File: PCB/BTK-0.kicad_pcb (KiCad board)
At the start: 4 copper layers, 169.2 x 105 mm, 92 parts, among them J1 USB_C_Receptacle_USB2.0_16P, J4 Conn_01x15, J5 Conn_01x15_Socket, SW1 EN, SW10 1,2, SW11 2,2, SW12 3,2, SW13 4,2, SW14 5,2, SW15 6,2, SW16 1,3, SW17 2,3, SW18 3,3, SW19 4,3, SW2 BOOT, SW20 5,3, SW21 6,3, SW22 1,4, SW23 2,4, SW24 3,4, SW25 4,4, SW26 5,4, SW27 6,4, SW28 1,4, SW29 2,4, SW3 RotaryEncoder_Switch_MP, SW30 3,4, SW31 4,4, SW32 5,4, SW33 6,4, SW4 1,1, SW5 2,1, SW6 3,1, SW7 4,1, SW8 5,1, SW9 6,1, U1 NCP1117-3.3_SOT223, U2 NCP1117-3.3_SOT223, U3 USBLC6-2SC6, U4 ESP32-C6-MINI-1, U5 TVS1400DRV

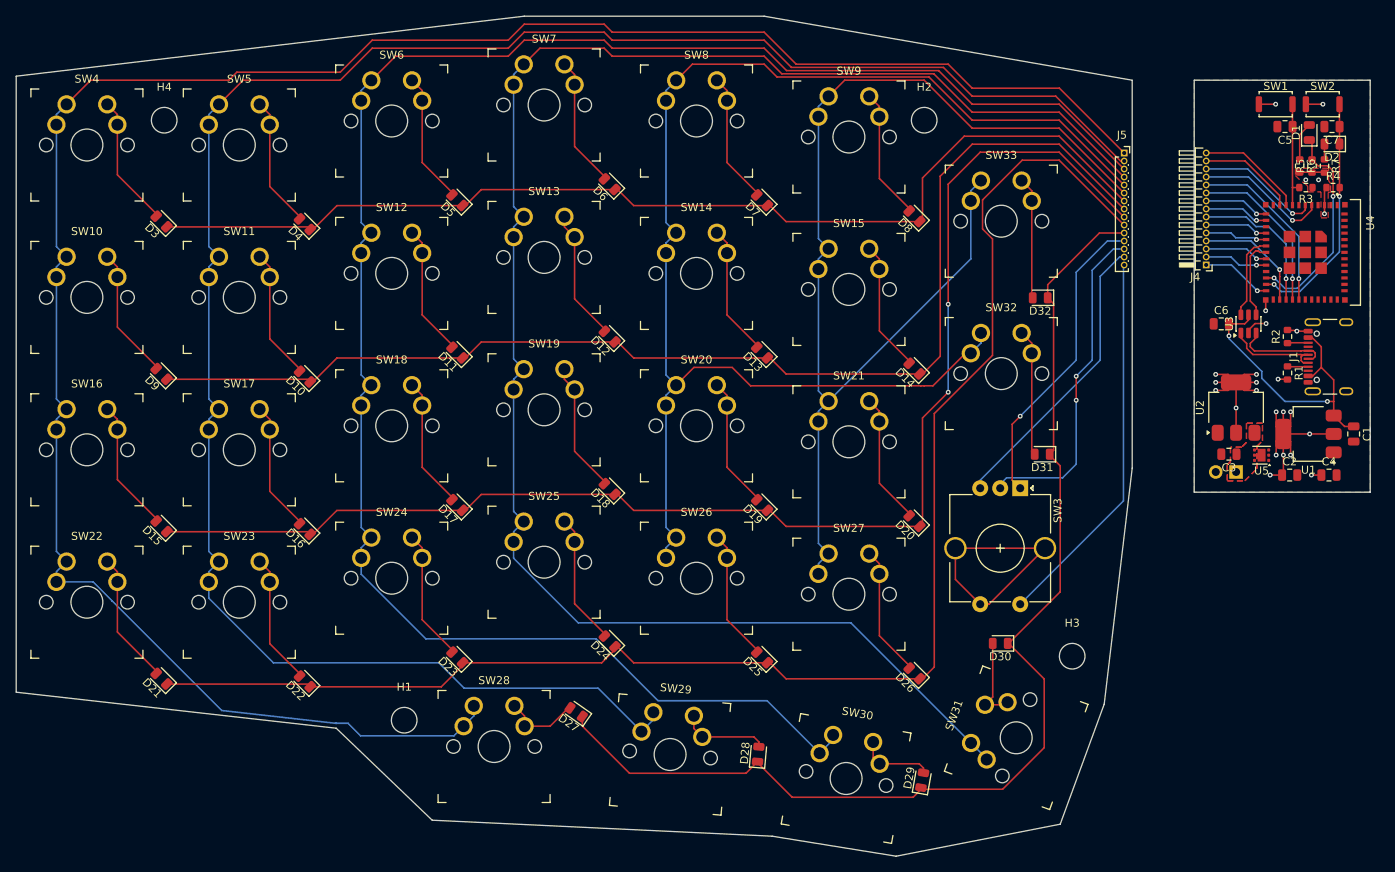
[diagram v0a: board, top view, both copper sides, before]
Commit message: fixed naming + control board more symmetrical, mcu to pin remap + mounting hole on control board
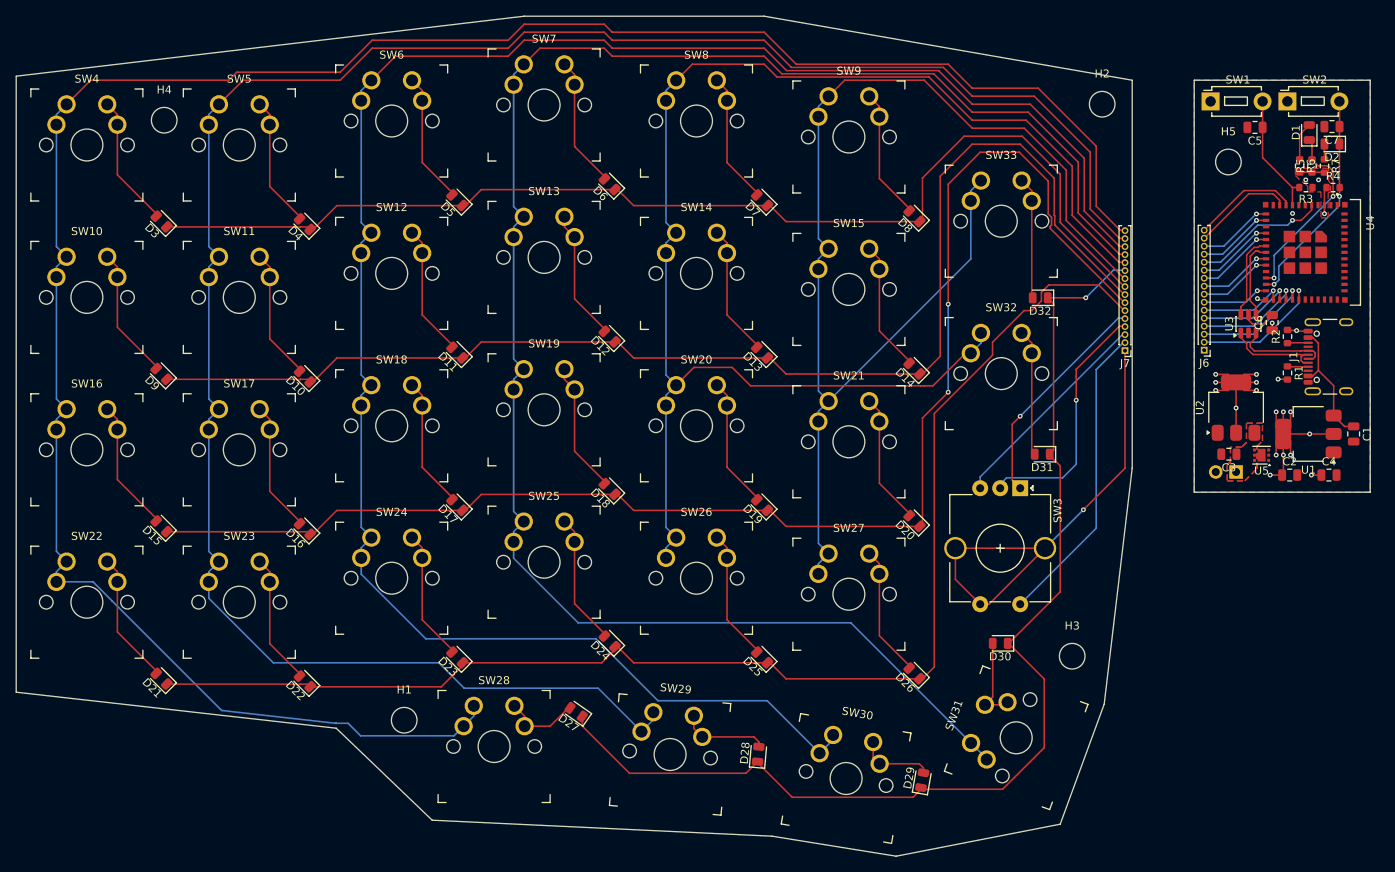
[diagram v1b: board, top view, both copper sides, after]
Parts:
- removed J4: Conn_01x15, Connector_PinHeader_1.00mm:PinHeader_1x15_P1.00mm_Horizontal
- removed J5: Conn_01x15_Socket, Connector_PinSocket_1.00mm:PinSocket_1x15_P1.00mm_Vertical
- added H5: MountingHole_Pad, MountingHole:MountingHole_3.2mm_M3_ISO7380, F.Cu at (133.0, 5.22)
- added J6: Conn_01x16_Pin, Connector_PinHeader_1.00mm:PinHeader_1x16_P1.00mm_Vertical, F.Cu at (130.0, 28.8)
- added J7: Conn_01x16_Socket, Connector_PinHeader_1.00mm:PinHeader_1x16_P1.00mm_Vertical, F.Cu at (120.1, 28.8)
- H1, H2, H3, H4: footprint MountingHole:MountingHole_3.2mm_M3 -> MountingHole:MountingHole_3.2mm_M3_ISO7380
- SW1, SW2: footprint Button_Switch_SMD:SW_Push_SPST_NO_Alps_SKRK -> Button_Switch_THT:SW_PUSH_1P1T_6x3.5mm_H4.3_APEM_MJTP1243
- moved H2 22.3 mm to (117.2, -2.00)
- moved SW1 8.14 mm to (130.8, -2.35)
- moved C6 6.37 mm to (138.5, 25.3), turned to 90 degrees
- moved SW2 4.42 mm to (140.4, -2.35)
- moved C5 3.75 mm to (136.3, 0.90)
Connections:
- D10 pad 1: /IO1 -> /IO14
- D11 pad 1: /IO1 -> /IO14
- D12 pad 1: /IO1 -> /IO14
- D13 pad 1: /IO1 -> /IO14
- D14 pad 1: /IO1 -> /IO14
- D15 pad 1: /IO21 -> /IO15
- D16 pad 1: /IO21 -> /IO15
- D17 pad 1: /IO21 -> /IO15
- D18 pad 1: /IO21 -> /IO15
- D19 pad 1: /IO21 -> /IO15
- D20 pad 1: /IO21 -> /IO15
- D21 pad 1: /IO6 -> /IO18
- D22 pad 1: /IO6 -> /IO18
- D23 pad 1: /IO6 -> /IO18
- D24 pad 1: /IO6 -> /IO18
- D25 pad 1: /IO6 -> /IO18
- D26 pad 1: /IO6 -> /IO18
- D27 pad 1: /IO7 -> /IO6
- D28 pad 1: /IO7 -> /IO6
- D29 pad 1: /IO7 -> /IO6
- D3 pad 1: /IO0 -> /IO7
- D30 pad 1: /IO7 -> /IO6
- D31 pad 1: /IO7 -> /IO6
- D32 pad 1: /IO7 -> /IO6
- D4 pad 1: /IO0 -> /IO7
- D5 pad 1: /IO0 -> /IO7
- D6 pad 1: /IO0 -> /IO7
- D7 pad 1: /IO0 -> /IO7
- D8 pad 1: /IO0 -> /IO7
- D9 pad 1: /IO1 -> /IO14
- SW12 pad 1: /IO3 -> /IO0
- SW13 pad 1: /IO2 -> /IO1
- SW14 pad 1: /IO23 -> /IO2
- SW15 pad 1: /IO22 -> /IO19
- SW18 pad 1: /IO3 -> /IO0
- SW19 pad 1: /IO2 -> /IO1
- SW20 pad 1: /IO23 -> /IO2
- SW21 pad 1: /IO22 -> /IO19
- SW24 pad 1: /IO3 -> /IO0
- SW25 pad 1: /IO2 -> /IO1
- SW26 pad 1: /IO23 -> /IO2
- SW27 pad 1: /IO22 -> /IO19
- SW3 pad B: /IO15 -> /IO22
- SW3 pad C: /IO14 -> /IO21
- SW3 pad S1: /IO18 -> /IO23
- SW30 pad 1: /IO3 -> /IO0
- SW31 pad 1: /IO2 -> /IO1
- SW32 pad 1: /IO23 -> /IO2
- SW33 pad 1: /IO22 -> /IO19
- SW6 pad 1: /IO3 -> /IO0
- SW7 pad 1: /IO2 -> /IO1
- SW8 pad 1: /IO23 -> /IO2
- SW9 pad 1: /IO22 -> /IO19
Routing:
- net /IO3: track 253.5 -> 0.00 mm, vias 1 -> 0
- net /IO19: track 0.00 -> 161.3 mm, vias 0 -> 1
- net /IO21: track 187.4 -> 44.6 mm, vias 3 -> 2
- net /IO15: track 44.6 -> 186.2 mm, vias 1 -> 3
- net /IO23: track 192.1 -> 54.9 mm
- net /IO22: track 163.2 -> 41.6 mm
- net /IO14: track 49.2 -> 168.6 mm, vias 3 -> 1
- net /IO18: track 56.6 -> 173.5 mm
- net /IO0: track 142.3 -> 255.1 mm
- net /IO1: track 159.7 -> 234.8 mm
- net /IO6: track 193.0 -> 149.2 mm, vias 1 -> 2
- net /IO2: track 234.2 -> 194.5 mm
- net GND: track 42.8 -> 65.1 mm, vias 6 -> 5
- net VBUS: track 38.5 -> 20.3 mm, vias 2 -> 0
- net /IO20: track 52.8 -> 39.9 mm
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
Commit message: fixing god knows what
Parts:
- D1, D2: footprint Diode_SMD:D_0805_2012Metric -> LED_SMD:LED_0805_2012Metric
- moved H1 3.16 mm to (27.0, 74.0)
- moved H2 2.14 mm to (118.0, 0.00)
- moved D32 0.61 mm to (109.6, 21.6), turned to 135 degrees
- moved H3 0.50 mm to (113.0, 67.0)
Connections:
- D10 pad 1: /IO14 -> /IO15
- D11 pad 1: /IO14 -> /IO15
- D12 pad 1: /IO14 -> /IO15
- D13 pad 1: /IO14 -> /IO15
- D14 pad 1: /IO14 -> /IO15
- D15 pad 1: /IO15 -> /IO18
- D16 pad 1: /IO15 -> /IO18
- D17 pad 1: /IO15 -> /IO18
- D18 pad 1: /IO15 -> /IO18
- D19 pad 1: /IO15 -> /IO18
- D20 pad 1: /IO15 -> /IO18
- D21 pad 1: /IO18 -> /IO19
- D22 pad 1: /IO18 -> /IO19
- D23 pad 1: /IO18 -> /IO19
- D24 pad 1: /IO18 -> /IO19
- D25 pad 1: /IO18 -> /IO19
- D26 pad 1: /IO18 -> /IO19
- D3 pad 1: /IO7 -> /IO14
- D4 pad 1: /IO7 -> /IO14
- D5 pad 1: /IO7 -> /IO14
- D6 pad 1: /IO7 -> /IO14
- D7 pad 1: /IO7 -> /IO14
- D8 pad 1: /IO7 -> /IO14
- D9 pad 1: /IO14 -> /IO15
- J6 pad 10: /IO19 -> /IO7
- J6 pad 6: /IO18 -> /IO19
- J6 pad 7: /IO15 -> /IO18
- J6 pad 8: /IO14 -> /IO15
- J6 pad 9: /IO7 -> /IO14
- J7 pad 10: /IO19 -> /IO7
- J7 pad 6: /IO18 -> /IO19
- J7 pad 7: /IO15 -> /IO18
- J7 pad 8: /IO14 -> /IO15
- J7 pad 9: /IO7 -> /IO14
- SW15 pad 1: /IO19 -> /IO7
- SW21 pad 1: /IO19 -> /IO7
- SW27 pad 1: /IO19 -> /IO7
- SW33 pad 1: /IO19 -> /IO7
- SW9 pad 1: /IO19 -> /IO7
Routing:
- net /IO15: track 186.2 -> 168.7 mm, vias 3 -> 1
- net /IO14: track 168.6 -> 151.3 mm
- net /IO19: track 161.3 -> 175.3 mm
- net Net-(D32-A): track 15.2 -> 3.07 mm
- net /IO18: track 173.5 -> 185.2 mm, vias 1 -> 3
- net VBUS: track 20.3 -> 31.1 mm
- net /IO7: track 151.9 -> 160.3 mm
- net (no net): track 0.26 -> 0.00 mm, vias 1 -> 0

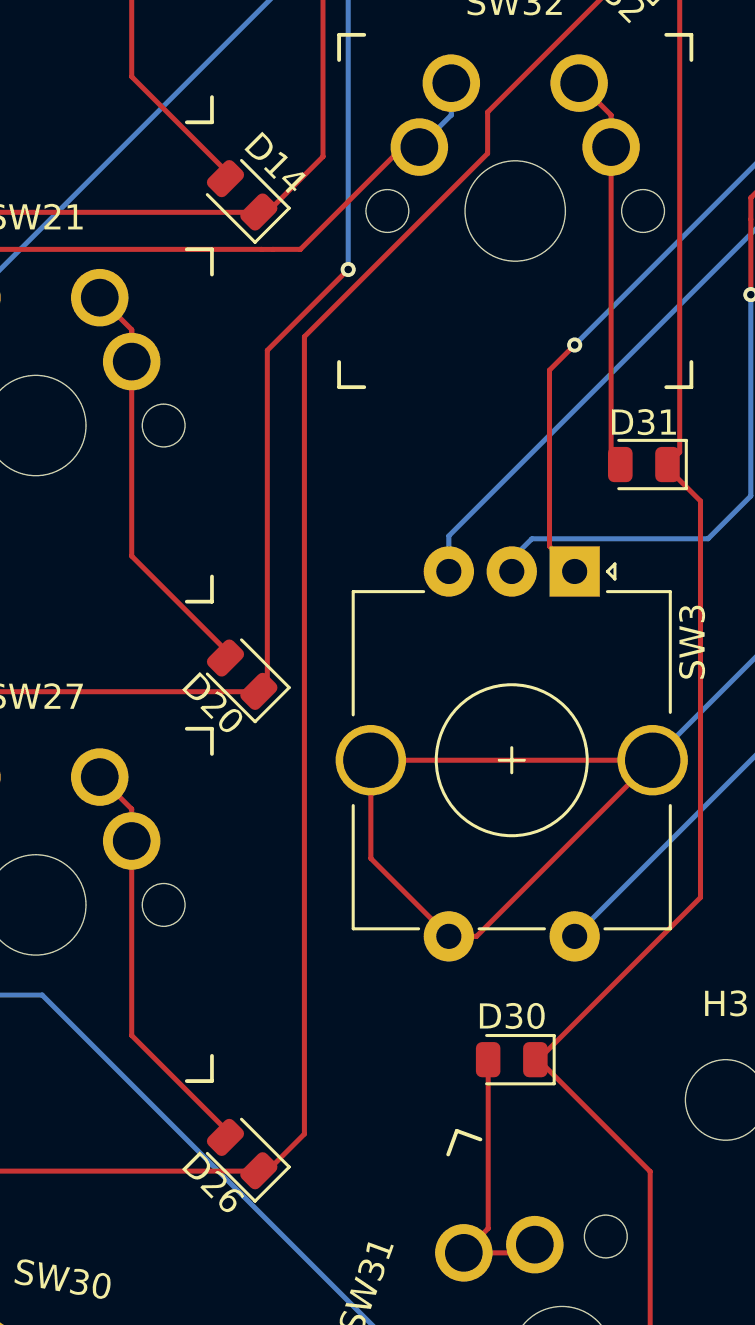
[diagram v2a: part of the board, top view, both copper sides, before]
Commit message: separate split pcb production files created
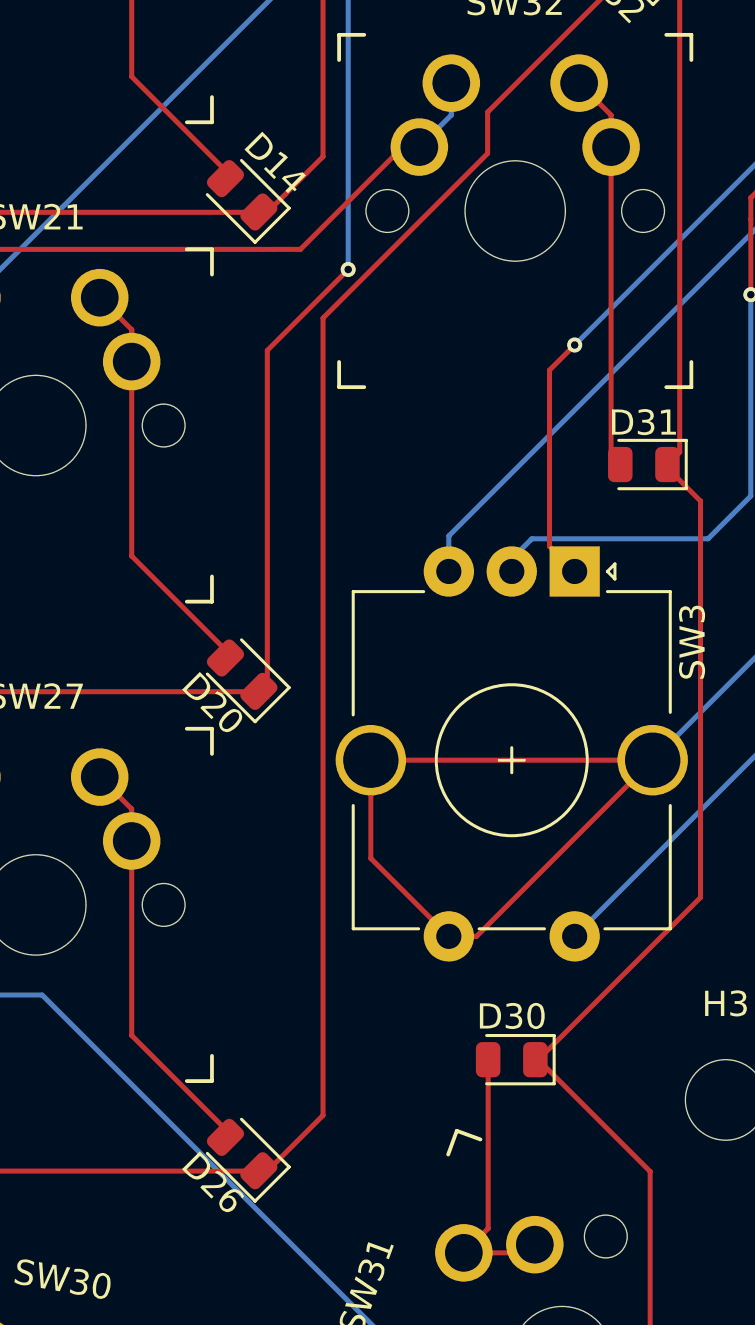
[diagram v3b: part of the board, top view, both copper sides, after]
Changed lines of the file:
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@@
+	)
+	(segment
+		(start 103.5405 29.390329)
+		(end 103.5405 27.746268)
+		(width 0.2)
+		(layer "F.Cu")
+		(net "/IO19")
+	)
+	(segment
+		(start 77.73639 69.827454)
+		(end 94.78639 69.827454)
+		(width 0.2)
+		(layer "F.Cu")
+		(net "/IO19")
+	)
+	(segment
+		(start 16.510076 70.488927)
+		(end 16.553176 70.532027)
+		(width 0.2)
+		(layer "F.Cu")
+		(net "/IO19")
+	)
+	(segment
+		(start 120 23.75)
+		(end 119.974695 23.75)
+		(width 0.2)
+		(layer "F.Cu")
+		(net "/IO19")
+	)
+	(segment
+		(start 119.374998 23.100305)
+		(end 119.799693 23.525)
+		(width 0.2)
+		(layer "F.Cu")
+		(net "/IO19")
+	)
+	(segment
+		(start 18.58639 70.827454)
+		(end 34.63639 70.827454)
+		(width 0.2)
+		(layer "F.Cu")
+		(net "/IO19")
+	)
+	(segment
+		(start 110.561762 20.725006)
+		(end 117.025006 20.725006)
+		(width 0.2)
+		(layer "F.Cu")
+		(net "/IO19")
+	)
+	(segment
+		(start 56.68639 65.827454)
+		(end 58.68639 67.827454)
+		(width 0.2)
+		(layer "F.Cu")
+		(net "/IO19")
+	)
+	(segment
+		(start 117.025006 20.725006)
+		(end 119.374998 23.074998)
+		(width 0.2)
+		(layer "F.Cu")
+		(net "/IO19")
+	)
+	(segment
+		(start 94.78639 69.827454)
+		(end 97 67.613844)
+		(width 0.2)
+		(layer "F.Cu")
+		(net "/IO19")
+	)
+	(segment
+		(start 37.63639 67.827454)
+		(end 54.68639 67.827454)
+		(width 0.2)
+		(layer "F.Cu")
+		(net "/IO19")
+	)
+	(segment
+		(start 119.799693 23.525)
+		(end 119.825 23.525)
+		(width 0.2)
+		(layer "F.Cu")
+		(net "/IO19")
+	)
+	(segment
+		(start 34.63639 70.827454)
+		(end 37.63639 67.827454)
+		(width 0.2)
+		(layer "F.Cu")
+		(net "/IO19")
+	)
+	(segment
+		(start 16.994084 70.532027)
+		(end 17.037184 70.488927)
+		(width 0.2)
+		(layer "F.Cu")
+		(net "/IO19")
+	)
+	(segment
+		(start 138.635 21.31373)
+		(end 138.635002 21.313728)
+		(width 0.2)
+		(layer "F.Cu")
+		(net "/IO19")
+	)
+	(segment
+		(start 120.099998 23.799998)
+		(end 120.099998 23.800001)
+		(width 0.2)
+		(layer "F.Cu")
+		(net "/IO19")
+	)
+	(segment
+		(start 16.553176 70.532027)
+		(end 16.994084 70.532027)
+		(width 0.2)
+		(layer "F.Cu")
+		(net "/IO19")
+	)
+	(segment
+		(start 138.635 22.42)
+		(end 138.635 21.31373)
+		(width 0.2)
+		(layer "F.Cu")
+		(net "/IO19")
+	)
+	(segment
+		(start 54.68639 67.827454)
+		(end 56.68639 65.827454)
+		(width 0.2)
+		(layer "F.Cu")
+		(net "/IO19")
 	)
 	(segment
@@
 	)
 	(segment
-		(start 94.78639 69.827454)
-		(end 96.260527 68.353317)
-		(width 0.2)
-		(layer "F.Cu")
-		(net "/IO19")
-	)
-	(segment
-		(start 96.260527 36.670302)
-		(end 103.5405 29.390329)
-		(width 0.2)
-		(layer "F.Cu")
-		(net "/IO19")
-	)
-	(segment
-		(start 117.025006 20.725006)
-		(end 119.374998 23.074998)
-		(width 0.2)
-		(layer "F.Cu")
-		(net "/IO19")
-	)
-	(segment
-		(start 120 23.75)
-		(end 119.974695 23.75)
+		(start 97 67.613844)
+		(end 97 35.930829)
+		(width 0.2)
+		(layer "F.Cu")
+		(net "/IO19")
+	)
+	(segment
+		(start 119.825 23.525)
+		(end 120.099998 23.799998)
 		(width 0.2)
 		(layer "F.Cu")
@@
 	)
 	(segment
-		(start 37.63639 67.827454)
-		(end 54.68639 67.827454)
-		(width 0.2)
-		(layer "F.Cu")
-		(net "/IO19")
-	)
-	(segment
-		(start 54.68639 67.827454)
-		(end 56.68639 65.827454)
-		(width 0.2)
-		(layer "F.Cu")
-		(net "/IO19")
-	)
-	(segment
-		(start 16.510076 70.488927)
-		(end 16.553176 70.532027)
-		(width 0.2)
-		(layer "F.Cu")
-		(net "/IO19")
-	)
-	(segment
-		(start 119.374998 23.100305)
-		(end 119.799693 23.525)
-		(width 0.2)
-		(layer "F.Cu")
-		(net "/IO19")
-	)
-	(segment
-		(start 34.63639 70.827454)
-		(end 37.63639 67.827454)
-		(width 0.2)
-		(layer "F.Cu")
-		(net "/IO19")
-	)
-	(segment
-		(start 119.799693 23.525)
-		(end 119.825 23.525)
-		(width 0.2)
-		(layer "F.Cu")
-		(net "/IO19")
-	)
-	(segment
-		(start 138.635 21.31373)
-		(end 138.635002 21.313728)
-		(width 0.2)
-		(layer "F.Cu")
-		(net "/IO19")
-	)
-	(segment
-		(start 103.5405 29.390329)
-		(end 103.5405 27.746268)
-		(width 0.2)
-		(layer "F.Cu")
-		(net "/IO19")
-	)
-	(segment
 		(start 0.6625 70.488927)
 		(end 16.510076 70.488927)
@@
 	)
 	(segment
-		(start 138.635 22.42)
-		(end 138.635 21.31373)
-		(width 0.2)
-		(layer "F.Cu")
-		(net "/IO19")
-	)
-	(segment
-		(start 96.260527 68.353317)
-		(end 96.260527 36.670302)
-		(width 0.2)
-		(layer "F.Cu")
-		(net "/IO19")
-	)
-	(segment
-		(start 120.099998 23.799998)
-		(end 120.099998 23.800001)
-		(width 0.2)
-		(layer "F.Cu")
-		(net "/IO19")
-	)
-	(segment
-		(start 16.553176 70.532027)
-		(end 16.994084 70.532027)
+		(start 58.68639 67.827454)
+		(end 75.73639 67.827454)
+		(width 0.2)
+		(layer "F.Cu")
+		(net "/IO19")
+	)
+	(segment
+		(start 103.5405 27.746268)
+		(end 110.561762 20.725006)
+		(width 0.2)
+		(layer "F.Cu")
+		(net "/IO19")
+	)
+	(segment
+		(start 97 35.930829)
+		(end 103.5405 29.390329)
 		(width 0.2)
 		(layer "F.Cu")
@@
 	)
 	(segment
-		(start 103.5405 27.746268)
-		(end 110.561762 20.725006)
-		(width 0.2)
-		(layer "F.Cu")
-		(net "/IO19")
-	)
-	(segment
-		(start 18.58639 70.827454)
-		(end 34.63639 70.827454)
-		(width 0.2)
-		(layer "F.Cu")
-		(net "/IO19")
-	)
-	(segment
-		(start 56.68639 65.827454)
-		(end 58.68639 67.827454)
-		(width 0.2)
-		(layer "F.Cu")
-		(net "/IO19")
-	)
-	(segment
-		(start 119.825 23.525)
-		(end 120.099998 23.799998)
-		(width 0.2)
-		(layer "F.Cu")
-		(net "/IO19")
-	)
-	(segment
 		(start 18.247863 70.488927)
 		(end 18.58639 70.827454)
 		(width 0.2)
 		(layer "F.Cu")
-		(net "/IO19")
-	)
-	(segment
-		(start 77.73639 69.827454)
-		(end 94.78639 69.827454)
-		(width 0.2)
-		(layer "F.Cu")
-		(net "/IO19")
-	)
-	(segment
-		(start 16.994084 70.532027)
-		(end 17.037184 70.488927)
-		(width 0.2)
-		(layer "F.Cu")
-		(net "/IO19")
-	)
-	(segment
-		(start 110.561762 20.725006)
-		(end 117.025006 20.725006)
-		(width 0.2)
-		(layer "F.Cu")
-		(net "/IO19")
-	)
-	(segment
-		(start 58.68639 67.827454)
-		(end 75.73639 67.827454)
-		(width 0.2)
-		(layer "F.Cu")
